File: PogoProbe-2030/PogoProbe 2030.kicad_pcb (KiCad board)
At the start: 2 copper layers, 22 x 36 mm, 12 parts, among them J1 Conn_ARM_SWD_TagConnect_TC203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

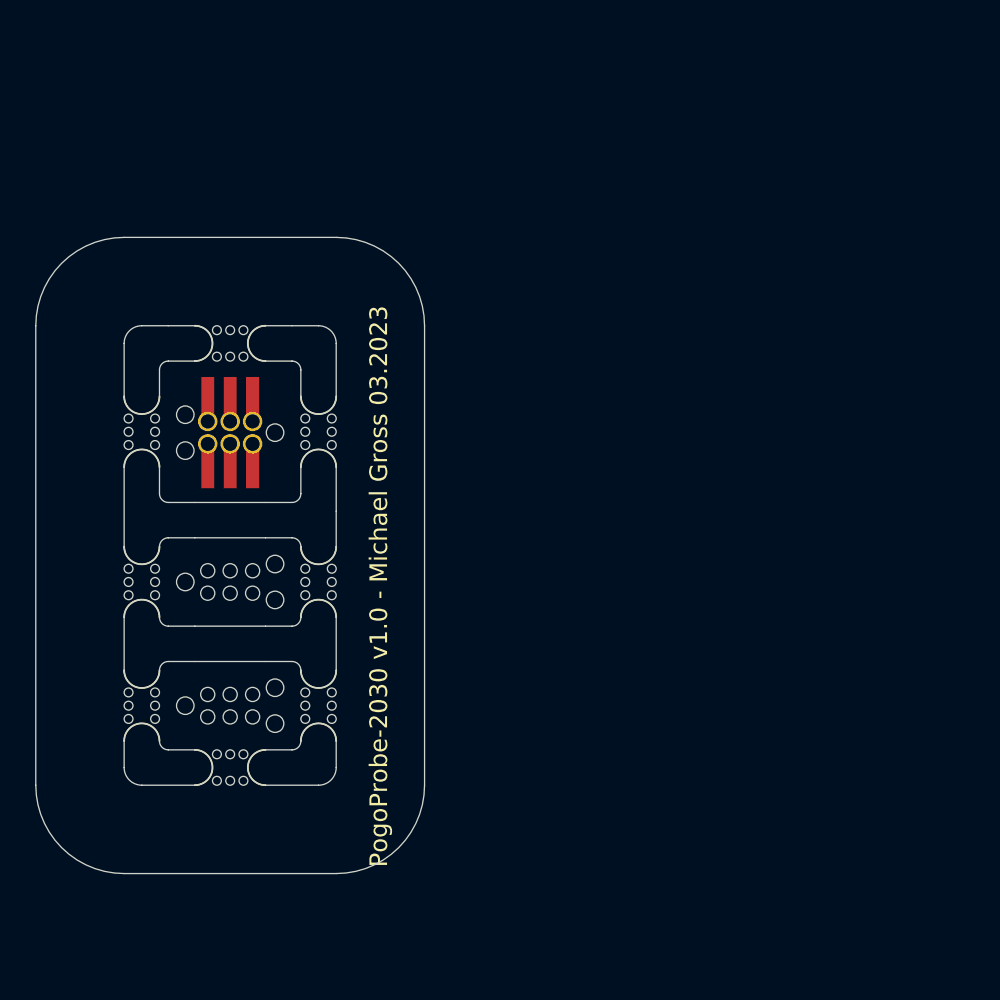
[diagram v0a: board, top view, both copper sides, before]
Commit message: Drop files from .gitignore
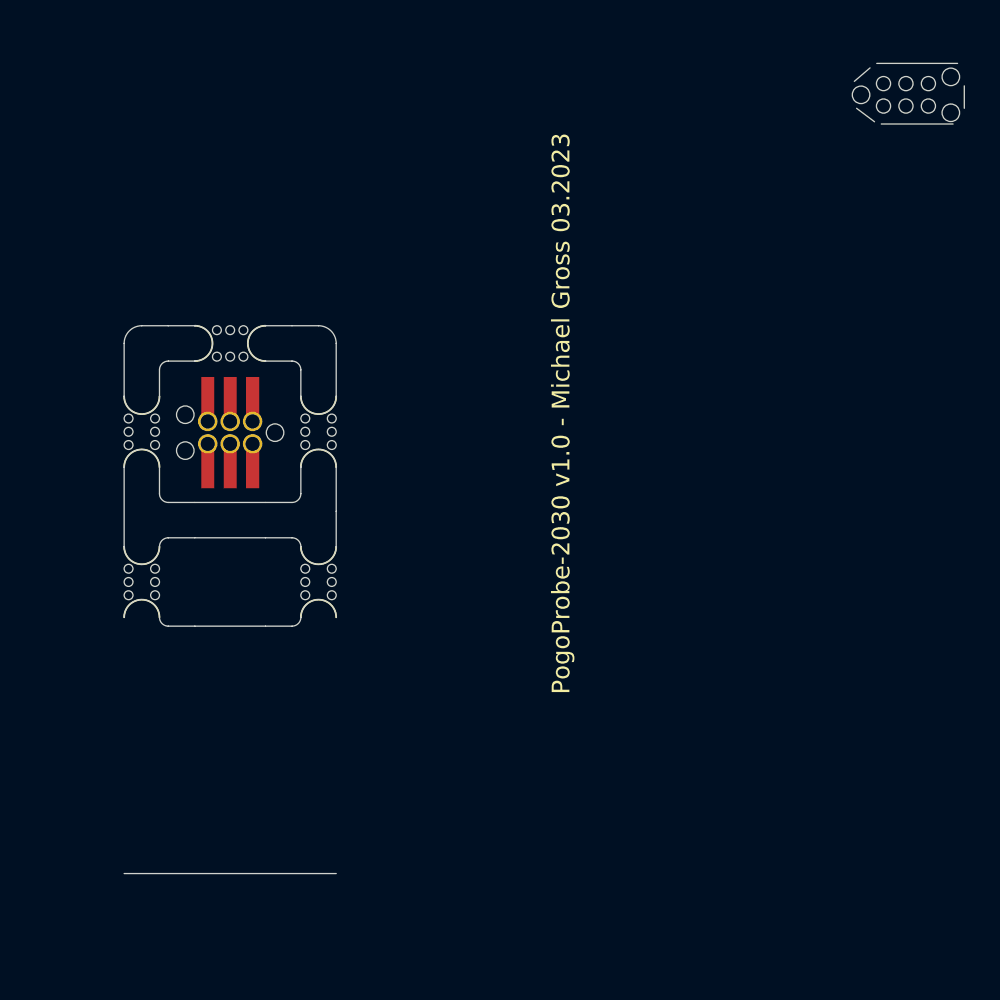
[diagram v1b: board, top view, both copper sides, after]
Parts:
- removed the J1 at (112.0, 133.5)
- removed the mouse-bite-2mm-slot at (117.0, 133.5)
- removed the mouse-bite-2mm-slot at (112.0, 137.0)
- removed the mouse-bite-2mm-slot at (107.0, 133.5)
- moved J1 47.1 mm to (150.2, 98.9)
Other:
- board size 22 x 36 mm -> 47.5 x 45.8 mm
